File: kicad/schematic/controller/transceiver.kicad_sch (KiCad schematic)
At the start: 29 parts, among them J6 SMA, U7 NRF24L01, U8 RFX2401C, Y3 16MHz

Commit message: feat(pcb): pcb wip
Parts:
- Y3: footprint (none) -> common:Crystal_3225
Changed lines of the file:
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@@
 			)
 		)
-		(property "Footprint" ""
+		(property "Footprint" "common:Crystal_3225"
 			(at 106.68 93.98 0)
 			(effects

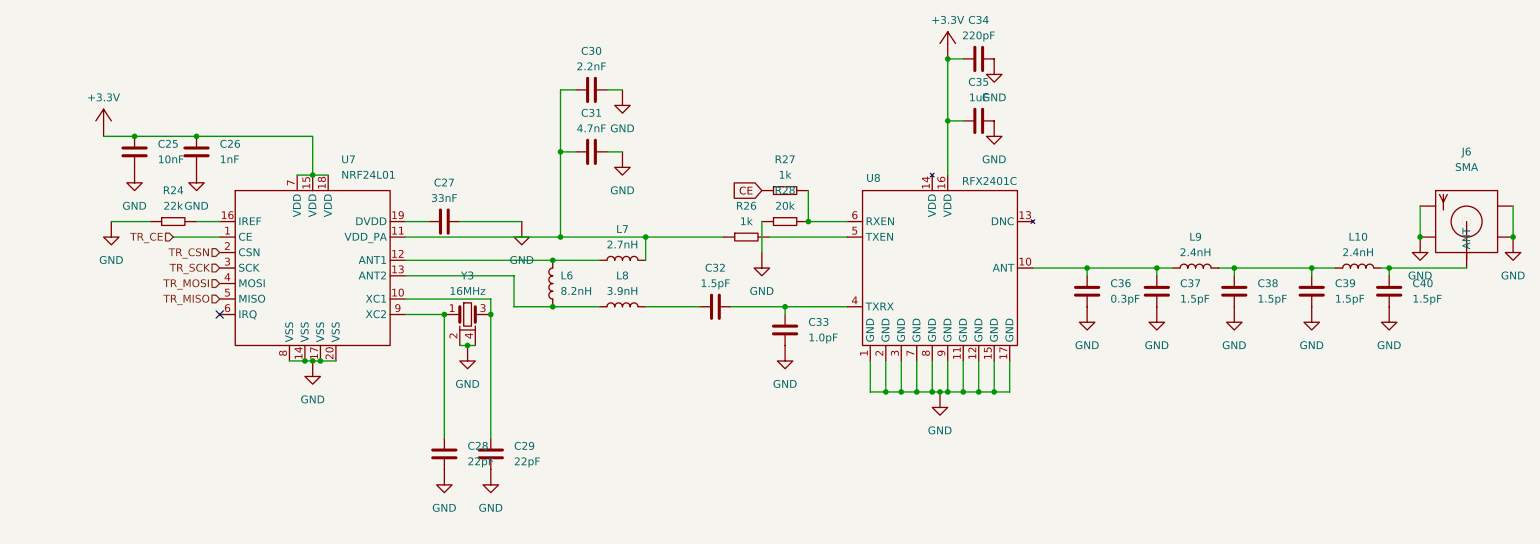
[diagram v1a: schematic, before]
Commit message: feat(schematic): cleanup controller
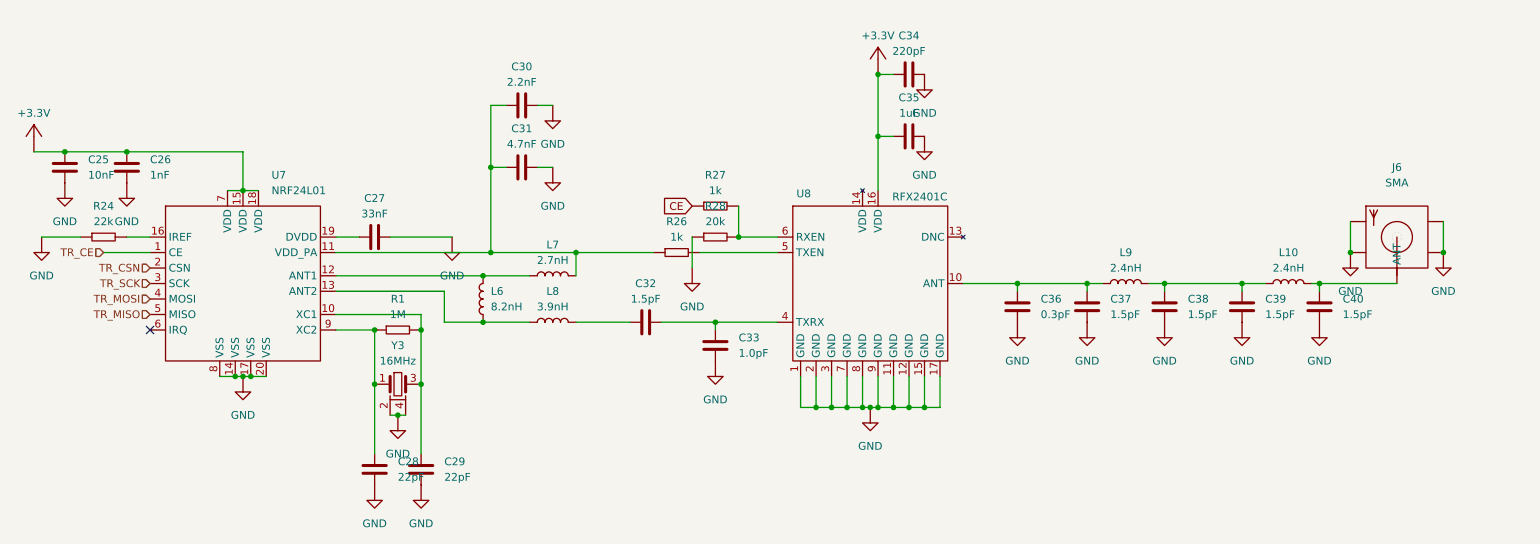
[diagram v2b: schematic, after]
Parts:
- added R1: 1M, common:R_0603, symbol common:Resistor
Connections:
- net at C29.2, U7.10 (XC1), Y3.3: now also R1.2
- net at C28.2, U7.9 (XC2), Y3.1: now also R1.1
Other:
- moved on the sheet: C25, C26, C27, C28, C29, C30, C31, C32, C33, C34, C35, C36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

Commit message: update controller pcb
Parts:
- C25: Ext. Price (none) -> 0.16; LCSC Part (none) -> C1589; Manufacturer (none) -> Samsung Electro-Mechanics; Manufacturer Part (none) -> CL10B103KB8NNNC; Unit Price (none) -> 0.0031
- C26: Ext. Price (none) -> 0.14; LCSC Part (none) -> C1588; Manufacturer (none) -> Samsung Electro-Mechanics; Manufacturer Part (none) -> CL10B102KB8NNNC; Unit Price (none) -> 0.0027
- C27: Ext. Price (none) -> 0.12; LCSC Part (none) -> C599735; Manufacturer (none) -> KEMET; Manufacturer Part (none) -> C0603C333K4RAC7867; Unit Price (none) -> 0.0119
- C28, C29: value 22pF -> 12pF; Ext. Price (none) -> 0.27; LCSC Part (none) -> C107034; Manufacturer (none) -> YAGEO; Manufacturer Part (none) -> CC0603JRNPO9BN120; Unit Price (none) -> 0.0027
- C30: Ext. Price (none) -> 0.19; LCSC Part (none) -> C33353; Manufacturer (none) -> Samsung Electro-Mechanics; Manufacturer Part (none) -> CL10C222JB8NNNC; Unit Price (none) -> 0.0093
- C31: Ext. Price (none) -> 0.22; LCSC Part (none) -> C1621; Manufacturer (none) -> Samsung Electro-Mechanics; Manufacturer Part (none) -> CL10B472KB8NNNC; Unit Price (none) -> 0.0043
- C32, C37, C38, C39, C40: Ext. Price (none) -> 0.23; LCSC Part (none) -> C376772; Manufacturer (none) -> CCTC; Manufacturer Part (none) -> TCC0603COG1R5C500CT; Unit Price (none) -> 0.0023
- C33: Ext. Price (none) -> 0.23; LCSC Part (none) -> C5137611; Manufacturer (none) -> FOJAN; Manufacturer Part (none) -> FCC0603N1R0C500CT; Unit Price (none) -> 0.0023
- C34: Ext. Price (none) -> 0.26; LCSC Part (none) -> C107081; Manufacturer (none) -> YAGEO; Manufacturer Part (none) -> CC0603KRX7R9BB221; Unit Price (none) -> 0.0026
- C35: Ext. Price (none) -> 0.05; LCSC Part (none) -> C26413; Manufacturer (none) -> Samsung Electro-Mechanics; Manufacturer Part (none) -> CL10A105KP8NNNC; Unit Price (none) -> 0.0048
- C36: Ext. Price (none) -> 0.35; LCSC Part (none) -> C5375816; Manufacturer (none) -> CCTC; Manufacturer Part (none) -> TCC0603COG0R3B500CT; Unit Price (none) -> 0.0035
- J6: Ext. Price (none) -> 3.21; LCSC Part (none) -> AliExpress; Manufacturer (none) -> JX; Manufacturer Part (none) -> SMA PCB; Unit Price (none) -> 3.21
- L10, L9: Ext. Price (none) -> 0.60; LCSC Part (none) -> C395082; Manufacturer (none) -> FH; Manufacturer Part (none) -> VHF160808H2N4ST; Unit Price (none) -> 0.006
- L6: Ext. Price (none) -> 0.51; LCSC Part (none) -> C412032; Manufacturer (none) -> Sunltech; Manufacturer Part (none) -> SCC1608C8N2JSP; Unit Price (none) -> 0.0102
- L7: Ext. Price (none) -> 0.26; LCSC Part (none) -> C5252358; Manufacturer (none) -> Chilisin; Manufacturer Part (none) -> BSCH001608082N7S00; Unit Price (none) -> 0.0128
- L8: Ext. Price (none) -> 0.40; LCSC Part (none) -> C964023; Manufacturer (none) -> HYHONGYEX; Manufacturer Part (none) -> HBLS1608-3N9S; Unit Price (none) -> 0.008
- R1: Ext. Price (none) -> 0.75; LCSC Part (none) -> C6949223; Manufacturer (none) -> YAGEO; Manufacturer Part (none) -> PA0603FRP070R001L; Unit Price (none) -> 0.1507
- R24: Ext. Price (none) -> 0.08; LCSC Part (none) -> C2907128; Manufacturer (none) -> FOJAN; Manufacturer Part (none) -> FRC0603J223 TS; Unit Price (none) -> 0.0008
- R26, R27: Ext. Price (none) -> 0.07; LCSC Part (none) -> C2907113; Manufacturer (none) -> FOJAN; Manufacturer Part (none) -> FRC0603J102 TS; Unit Price (none) -> 0.0007
- R28: Ext. Price (none) -> 0.07; LCSC Part (none) -> C2907124; Manufacturer (none) -> FOJAN; Manufacturer Part (none) -> FRC0603J203 TS; Unit Price (none) -> 0.0007
- U7: Ext. Price (none) -> 2.05; LCSC Part (none) -> C8791; Manufacturer (none) -> NORDIC; Manufacturer Part (none) -> NRF24L01P-R; Unit Price (none) -> 2.0451
- U8: Ext. Price (none) -> 0.77; LCSC Part (none) -> C19213; Manufacturer (none) -> SKYWORKS; Manufacturer Part (none) -> RFX2401C; Unit Price (none) -> 0.7744
- Y3: Ext. Price (none) -> 0.59; LCSC Part (none) -> C13738; Manufacturer (none) -> YXC Crystal Oscillators; Manufacturer Part (none) -> X322516MLB4SI; Unit Price (none) -> 0.059
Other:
- moved on the sheet: C28
